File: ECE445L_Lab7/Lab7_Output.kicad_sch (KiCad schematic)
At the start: 4 parts, among them Q1 IRLD024PBF, U2 Adafruit ST7735R

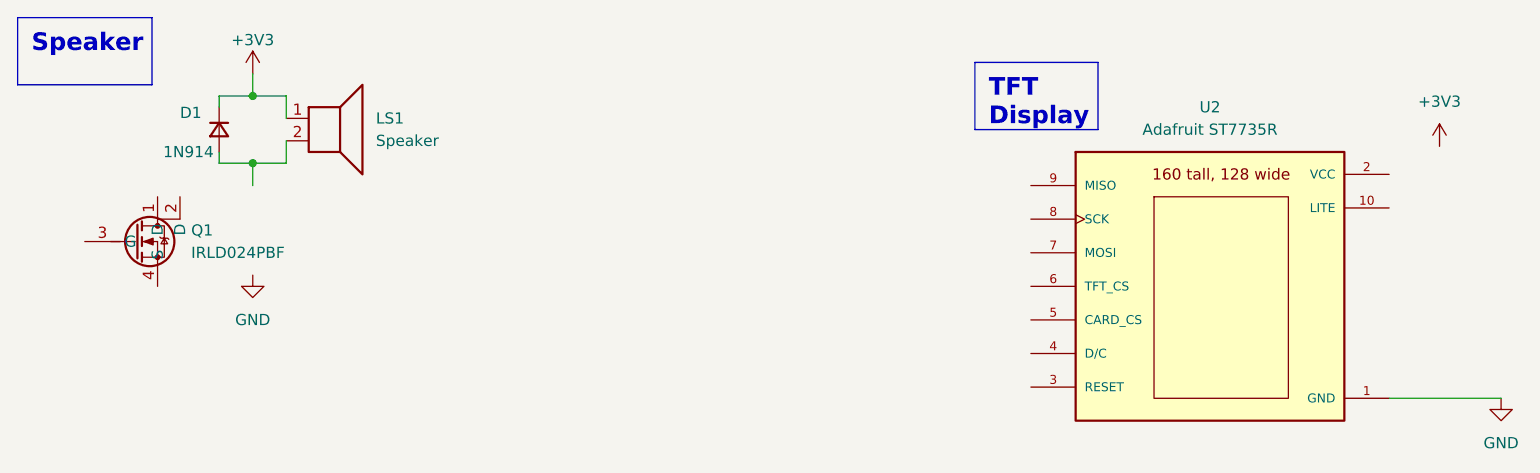
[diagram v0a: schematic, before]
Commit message: update all symbols and re-sync footprints in the KiCad projects
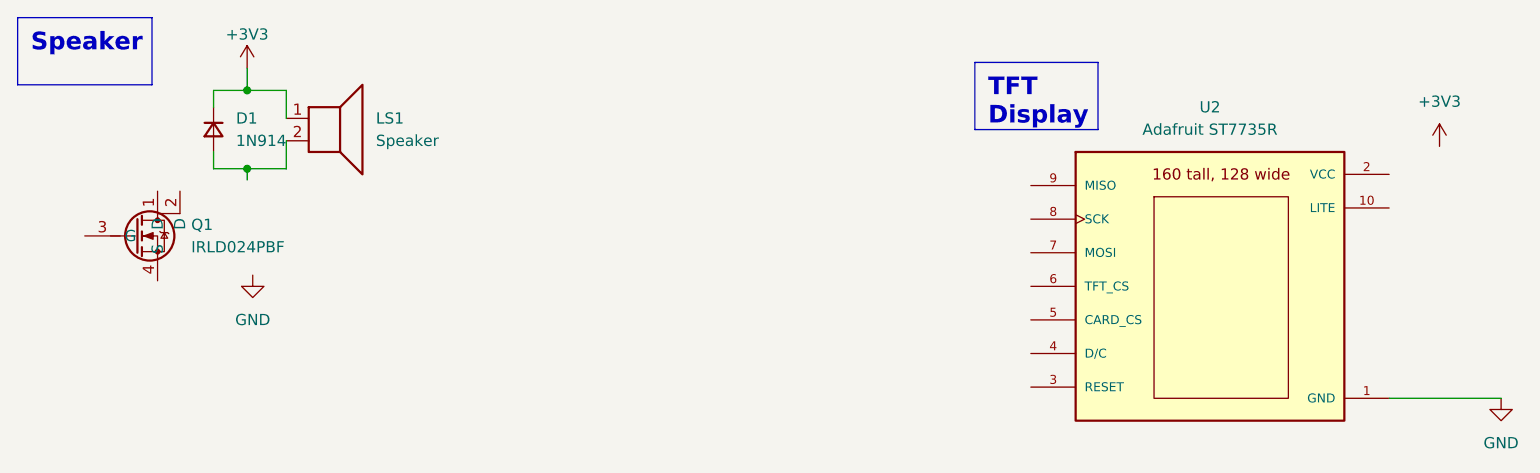
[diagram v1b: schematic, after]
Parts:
- removed D1: 1N914, ECE445L:D_P6.35mm_Horizontal, symbol ECE445L:D_Small
- added D1: 1N914, Diode_THT:D_5W_P12.70mm_Horizontal, symbol Device:D_Small
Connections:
- net +3V3: now also D1.1 (K)
- net at LS1.2: now also D1.2 (A)
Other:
- moved on the sheet: Q1
